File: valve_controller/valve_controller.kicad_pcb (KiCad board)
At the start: 2 copper layers, 9 parts, among them U1 LAN8720A, U2 ADS1115IDGS, U3 MCP4728, U5 LM2596S-5, U6 LDO-LM7805MPX/NOPB, U7 ESP32-S3, U8 TVS-SMDB03CE3

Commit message: First layout  of pcb
Ready for review
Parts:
- added C1: 100nF, Capacitor_SMD:C_0805_2012Metric_Pad1.18x1.45mm_HandSolder, F.Cu at (106.3, 51.9)
- added C2: 100nF, Capacitor_SMD:C_0805_2012Metric_Pad1.18x1.45mm_HandSolder, F.Cu at (106.3, 54.9)
- added J10: 643260100604, 643260100604:643260100604, F.Cu at (182.2, 140.5)
- added J11: 643260100604, 643260100604:643260100604, F.Cu at (182.2, 120.8)
- added J4: 643260100604, 643260100604:643260100604, F.Cu at (117.1, 140.5)
- added J5: 643260100604, 643260100604:643260100604, F.Cu at (117.1, 120.8)
- added J6: 643260100604, 643260100604:643260100604, F.Cu at (138.8, 140.5)
- added J7: 643260100604, 643260100604:643260100604, F.Cu at (138.8, 120.8)
- added J8: 643260100604, 643260100604:643260100604, F.Cu at (160.5, 140.5)
- added J9: 643260100604, 643260100604:643260100604, F.Cu at (160.5, 120.8)
- added R10: 1k, Resistor_SMD:R_0201_0603Metric, F.Cu at (109.9, 51.3)
- added R11: 1k, Resistor_SMD:R_0201_0603Metric, F.Cu at (109.9, 53.0)
- added SW1: TS09-63-25-WT-160-SMT-TR, Button_Switch_SMD:SW_DIP_SPSTx01_Slide_6.7x4.1mm_W8.61mm_P2.54mm_LowProfile, F.Cu at (110.2, 41.6)
- added SW2: TS09-63-25-WT-160-SMT-TR, Button_Switch_SMD:SW_DIP_SPSTx01_Slide_6.7x4.1mm_W8.61mm_P2.54mm_LowProfile, F.Cu at (110.2, 47.5)
- moved D1 24.7 mm to (181.0, 89.5)
- moved D2 24.7 mm to (181.0, 95.0)
- moved U1 24.7 mm to (154.5, 90.5)
- moved U2 24.7 mm to (148.8, 76.5)
- moved U3 24.7 mm to (153.4, 83.0)
- moved U5 24.7 mm to (138.4, 73.7)
- moved U6 24.7 mm to (168.8, 74.6)
- moved U7 24.7 mm to (161.5, 83.8)
- moved U8 24.7 mm to (157.0, 70.6)
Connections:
- U1 pad 5: unconnected-(U1-XTAL1/CLKIN-Pad5) -> /25MHZ
- U2 pad 10: /SCL_ADC1 -> /SCL
- U2 pad 2: /ALERT/RDY_ADC1 -> unconnected-(U2-ALERT/RDY-Pad2)
- U2 pad 9: /SDA_ADC1 -> /SDA
- U3 pad 2: /SCL_DAC1 -> /SCL
- U3 pad 3: /SDA_DAC1 -> /SDA
- U3 pad 5: /RDY_DAC1 -> unconnected-(U3-RDY/~{BSY}-Pad5)
- U7 pad 2: Net-(U7-VDD3P3-Pad2) -> +3V3
- U7 pad 20: unconnected-(U7-VDD3P3_RTC-Pad20) -> +3V3
- U7 pad 3: Net-(U7-VDD3P3-Pad2) -> +3V3
- U7 pad 38: unconnected-(U7-GPIO33-Pad38) -> /SCL
- U7 pad 39: unconnected-(U7-GPIO34-Pad39) -> /SDA
- U7 pad 4: unconnected-(U7-CHIP_PU-Pad4) -> /CHIP_PU
- U7 pad 55: Net-(U7-VDDA-Pad55) -> +3V3
- U7 pad 56: Net-(U7-VDDA-Pad55) -> +3V3

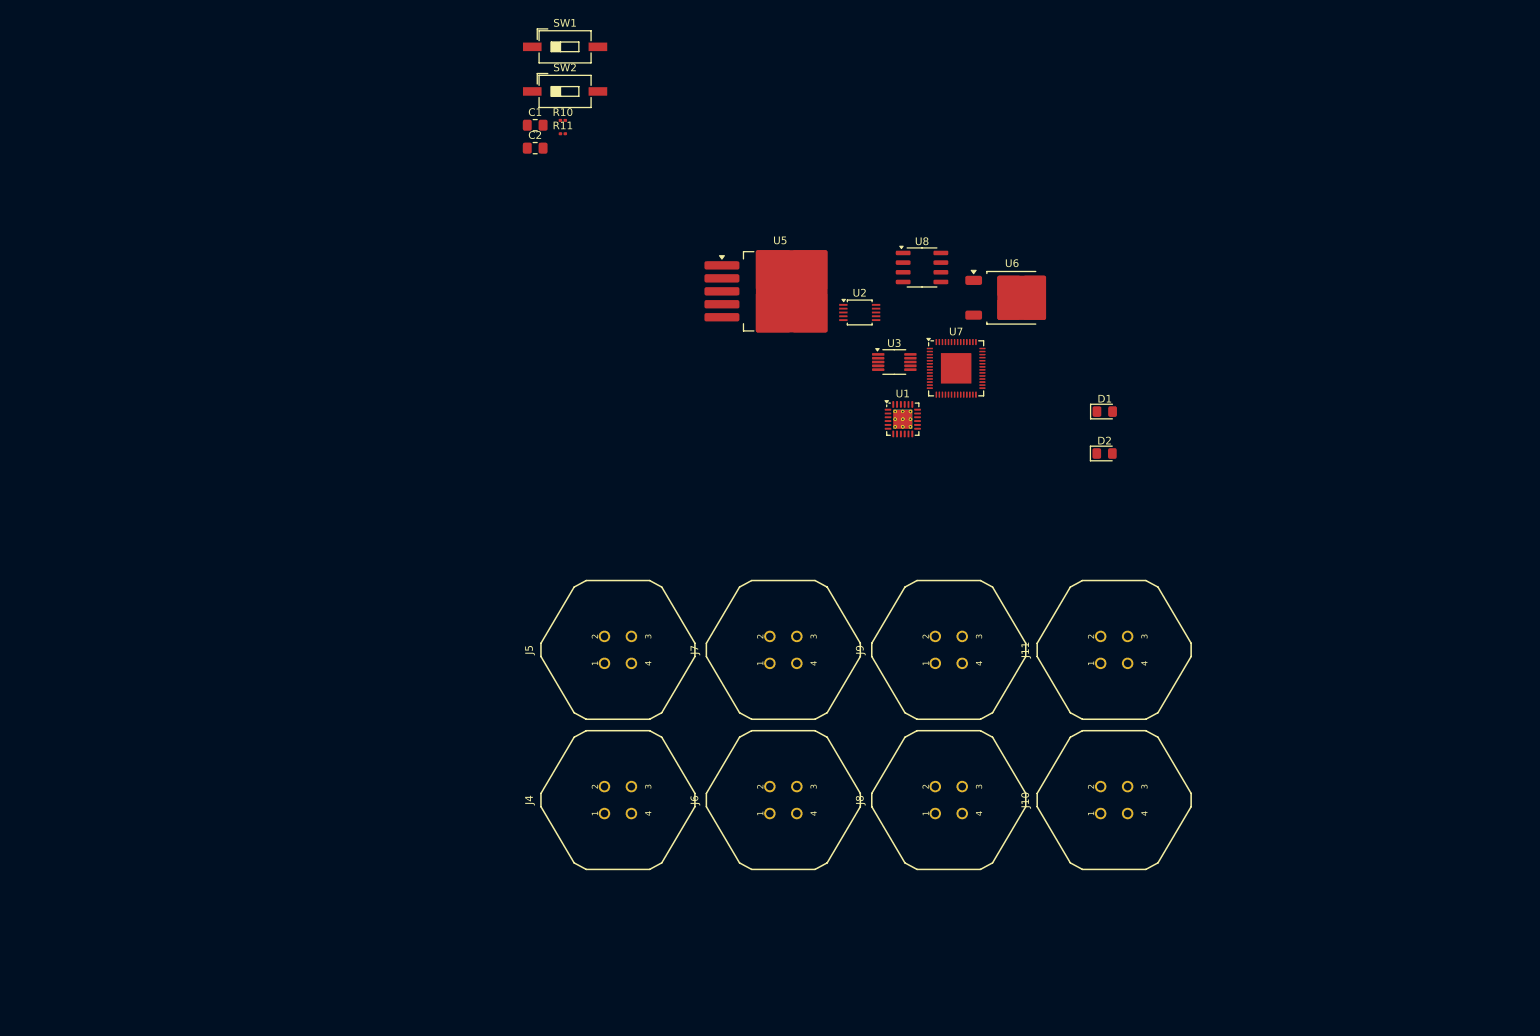
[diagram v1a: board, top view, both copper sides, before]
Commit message: Updated + ports
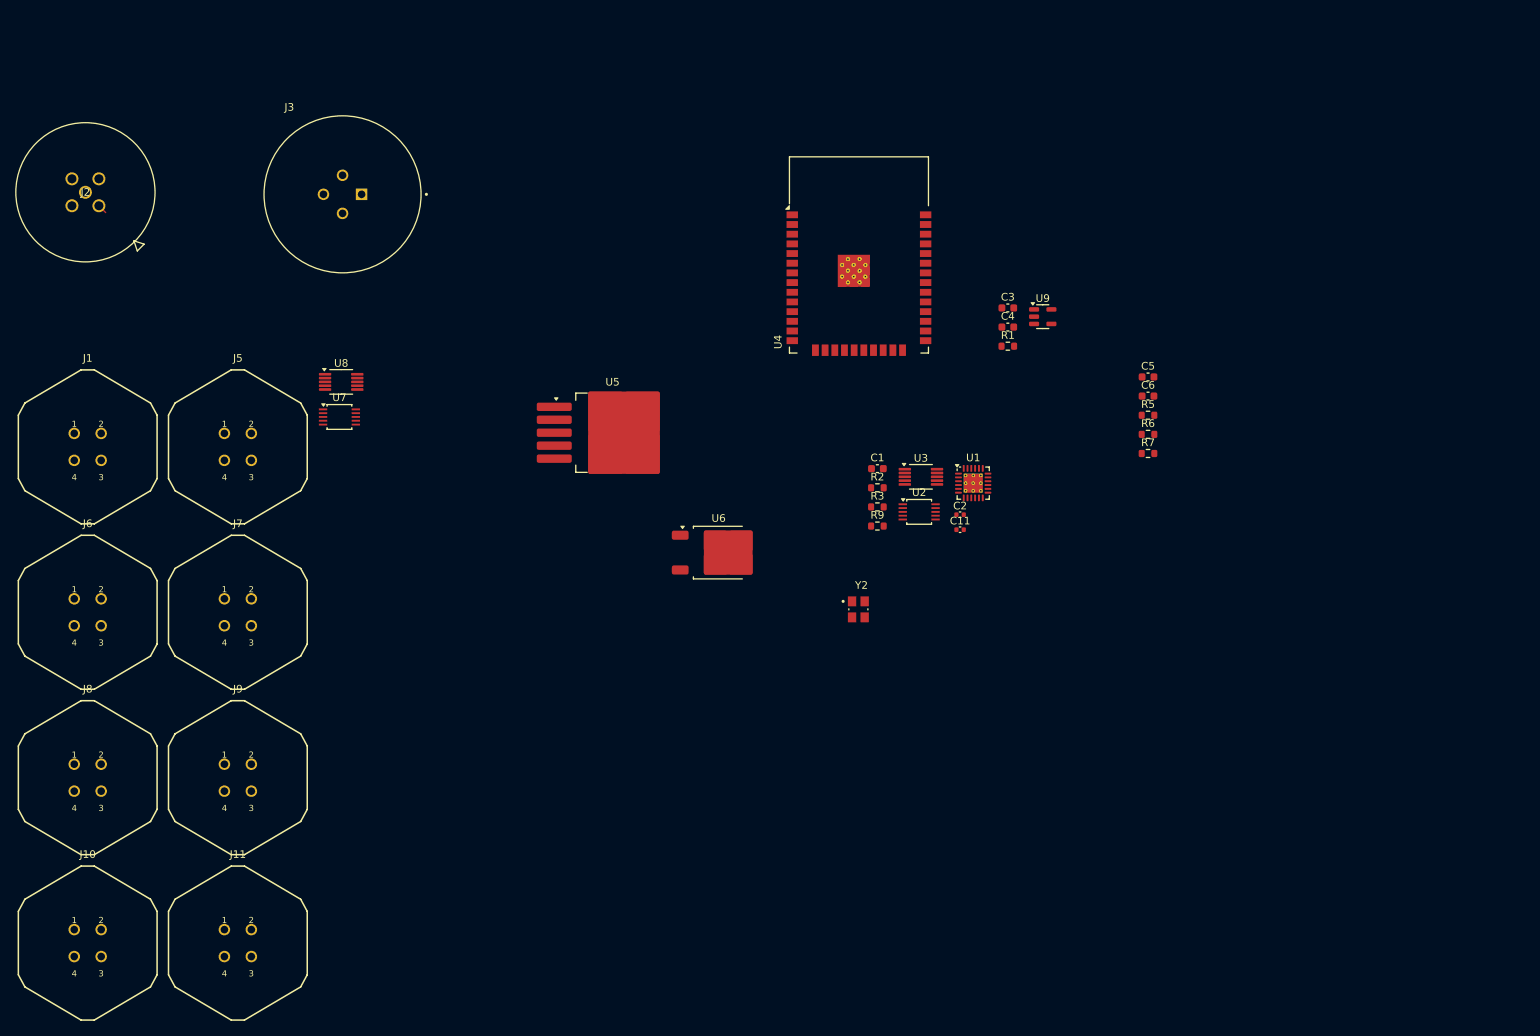
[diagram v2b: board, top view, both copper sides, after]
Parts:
- removed D1, D2: LED, LED_SMD:LED_0805_2012Metric_Pad1.15x1.40mm_HandSolder
- removed J4: 643260100604, 643260100604:643260100604
- removed R10, R11: 1k, Resistor_SMD:R_0201_0603Metric
- removed SW1, SW2: TS09-63-25-WT-160-SMT-TR, Button_Switch_SMD:SW_DIP_SPSTx01_Slide_6.7x4.1mm_W8.61mm_P2.54mm_LowProfile
- added C11: 0.1uF, Capacitor_SMD:C_0402_1005Metric, F.Cu at (162.0, 105.0)
- added C3: 22uF, Capacitor_SMD:C_0603_1608Metric, F.Cu at (168.3, 75.9)
- added C4: 22uF, Capacitor_SMD:C_0603_1608Metric, F.Cu at (168.3, 78.4)
- added C5: 1uF, Capacitor_SMD:C_0603_1608Metric, F.Cu at (186.7, 85.0)
- added C6: 470pF, Capacitor_SMD:C_0603_1608Metric, F.Cu at (186.7, 87.5)
- added J1: 643260100604, 643260100604:643260100604, F.Cu at (47.6, 94.1)
- added J2: T4143512051-000, T4143512051_000:CONN5_T4143512051, F.Cu at (45.5, 59.0)
- added J3: M12A-04PMMP-SF8001, M12A-04PMMP-SF8001:AMPHENOL_M12A-04PMMP-SF8001, F.Cu at (81.0, 61.0)
- added R1: 100k, Resistor_SMD:R_0603_1608Metric, F.Cu at (168.3, 80.9)
- added R2: 100k, Resistor_SMD:R_0603_1608Metric, F.Cu at (151.2, 99.5)
- added R3: 100k, Resistor_SMD:R_0603_1608Metric, F.Cu at (151.2, 102.0)
- added R5: 12.1k, Resistor_SMD:R_0603_1608Metric, F.Cu at (186.7, 90.0)
- added R6: 10k, Resistor_SMD:R_0603_1608Metric, F.Cu at (186.7, 92.5)
- added R7: 10k, Resistor_SMD:R_0603_1608Metric, F.Cu at (186.7, 95.0)
- added R9: 100k, Resistor_SMD:R_0603_1608Metric, F.Cu at (151.2, 104.5)
- added U4: ESP32-WROOM-32, RF_Module:ESP32-WROOM-32, F.Cu at (148.8, 71.9)
- added U9: AP2112K-3.3, Package_TO_SOT_SMD:SOT-23-5, F.Cu at (172.9, 77.0)
- added Y2: ASE-25.000MHZ-LC-T, ASE-25.000MHZ-LC-T:XTAL_ASE-25.000MHZ-LC-T, F.Cu at (148.7, 115.5)
- C1: value 100nF -> 22uF; footprint Capacitor_SMD:C_0805_2012Metric_Pad1.18x1.45mm_HandSolder -> Capacitor_SMD:C_0603_1608Metric
- C2: value 100nF -> 0.1uF; footprint Capacitor_SMD:C_0805_2012Metric_Pad1.18x1.45mm_HandSolder -> Capacitor_SMD:C_0402_1005Metric
- U7: value ESP32-S3 -> ADS1115IDGS; footprint Package_DFN_QFN:QFN-56-1EP_7x7mm_P0.4mm_EP4x4mm -> Package_SO:TSSOP-10_3x3mm_P0.5mm
- U8: value TVS-SMDB03CE3 -> MCP4728; footprint Package_SO:SOIC-8_3.9x4.9mm_P1.27mm -> Package_SO:MSOP-10_3x3mm_P0.5mm
- moved J10 136.0 mm to (47.6, 159.2), turned to 0 degrees
- moved J11 121.2 mm to (67.3, 159.2), turned to 0 degrees
- moved J8 113.0 mm to (47.6, 137.5), turned to 0 degrees
- moved J9 94.8 mm to (67.3, 137.5), turned to 0 degrees
- moved J6 94.5 mm to (47.6, 115.8), turned to 0 degrees
- moved U7 81.2 mm to (80.6, 90.2)
- moved U8 77.7 mm to (80.8, 85.6)
- moved C2 73.6 mm to (162.0, 103.0)
- moved J7 71.7 mm to (67.3, 115.8), turned to 0 degrees
- moved C1 63.6 mm to (151.2, 97.0)
- moved J5 56.5 mm to (67.3, 94.1), turned to 0 degrees
- moved U6 51.0 mm to (130.3, 108.0)
- moved U5 28.8 mm to (116.4, 92.3)
- moved U2 27.3 mm to (156.7, 102.7)
- moved U3 15.5 mm to (156.9, 98.1)
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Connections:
- C1 pad 1: GND -> +3V3
- C1 pad 2: /BOOT -> GND
- C2 pad 1: GND -> +3V3
- C2 pad 2: /CHIP_PU -> GND
- J10 pad 1: unconnected-(J10-Pad1) -> /AIN2_ADC1
- J10 pad 4: unconnected-(J10-Pad4) -> /ANOUT2_DAC1
- J11 pad 1: unconnected-(J11-Pad1) -> /AIN3_ADC1
- J11 pad 4: unconnected-(J11-Pad4) -> /ANOUT3_DAC1
- J5 pad 1: unconnected-(J5-Pad1) -> /AIN0_ADC0
- J5 pad 4: unconnected-(J5-Pad4) -> /ANOUT0_DAC0
- J6 pad 1: unconnected-(J6-Pad1) -> /AIN2_ADC0
- J6 pad 4: unconnected-(J6-Pad4) -> /ANOUT2_DAC0
- J7 pad 1: unconnected-(J7-Pad1) -> /AIN3_ADC0
- J7 pad 4: unconnected-(J7-Pad4) -> /ANOUT3_DAC0
- J8 pad 1: unconnected-(J8-Pad1) -> /AIN0_ADC1
- J8 pad 4: unconnected-(J8-Pad4) -> /ANOUT0_DAC1
- J9 pad 1: unconnected-(J9-Pad1) -> /AIN1_ADC1
- J9 pad 4: unconnected-(J9-Pad4) -> /ANOUT1_DAC1
- U2 pad 4: /AIN0_ADC1 -> /AIN0_ADC0
- U2 pad 5: /AIN1_ADC1 -> /AIN1_ADC0
- U2 pad 6: /AIN2_ADC1 -> /AIN2_ADC0
- U2 pad 7: /AIN3_ADC1 -> /AIN3_ADC0
- U3 pad 6: /ANOUT0_DAC1 -> /ANOUT0_DAC0
- U3 pad 7: /ANOUT1_DAC1 -> /ANOUT1_DAC0
- U3 pad 8: /ANOUT2_DAC1 -> /ANOUT2_DAC0
- U3 pad 9: /ANOUT3_DAC1 -> /ANOUT3_DAC0
- U7 pad 1: unconnected-(U7-LNA_IN-Pad1) -> GND
- U7 pad 10: unconnected-(U7-GPIO5-Pad10) -> /SCL
- U7 pad 2: +3V3 -> unconnected-(U7-ALERT/RDY-Pad2)
- U7 pad 3: +3V3 -> GND
- U7 pad 4: /CHIP_PU -> /AIN0_ADC1
- U7 pad 5: /REF_CLK -> /AIN1_ADC1
- U7 pad 6: unconnected-(U7-GPIO1-Pad6) -> /AIN2_ADC1
- U7 pad 7: unconnected-(U7-GPIO2-Pad7) -> /AIN3_ADC1
- U7 pad 8: unconnected-(U7-GPIO3-Pad8) -> +3V3
- U7 pad 9: unconnected-(U7-GPIO4-Pad9) -> /SDA
- U8 pad 1: +5V -> +3V3
- U8 pad 2: /USB_N -> /SCL
- U8 pad 3: /USB_P -> /SDA
- U8 pad 4: unconnected-(U8-Pad4) -> GND
- U8 pad 5: GND -> unconnected-(U8-RDY/~{BSY}-Pad5)
- U8 pad 6: GND -> /ANOUT0_DAC1
- U8 pad 7: GND -> /ANOUT1_DAC1
- U8 pad 8: GND -> /ANOUT2_DAC1

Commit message: Started pcb layout
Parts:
- removed U6: LDO-LM7805MPX/NOPB, Package_TO_SOT_SMD:TO-252-2
- added D1: WS2812B, LED_SMD:LED_WS2812B_PLCC4_5.0x5.0mm_P3.2mm, F.Cu at (156.7, 105.3)
- moved J2 137.0 mm to (182.5, 62.0)
- moved J11 126.8 mm to (139.8, 55.2), turned to 90 degrees
- moved J3 120.3 mm to (185.0, 121.5), turned to 180 degrees
- moved J10 98.7 mm to (139.2, 122.8), turned to 90 degrees
- moved J9 95.6 mm to (115.8, 55.2), turned to 90 degrees
- moved U7 75.9 mm to (153.4, 68.9), turned to 180 degrees
- moved J8 69.3 mm to (115.2, 122.8), turned to 90 degrees
- moved U8 67.0 mm to (146.6, 72.5), turned to 180 degrees
- moved J7 65.2 mm to (91.3, 55.2), turned to 90 degrees
- moved U5 61.0 mm to (176.6, 102.2), turned to 180 degrees
- moved J6 43.5 mm to (90.5, 122.8), turned to 90 degrees
- moved Y2 41.6 mm to (169.9, 79.8)
- moved J5 38.9 mm to (66.3, 55.2), turned to 90 degrees
- moved U2 35.3 mm to (146.6, 68.8)
- moved J1 33.8 mm to (65.5, 122.8), turned to 90 degrees
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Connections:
- J2 pad 2: /RX_N -> /RX_P
- U4 pad 13: /RXER -> /TXD0
- U4 pad 14: /MDIO -> /TXEN
- U4 pad 16: /CRS_DV -> /TXD1
- U4 pad 23: /RXD1 -> /MDIO
- U4 pad 24: unconnected-(U4-IO2-Pad24) -> /CRS_DV
- U4 pad 26: unconnected-(U4-IO4-Pad26) -> /RXER
- U4 pad 27: /RXD0 -> unconnected-(U4-IO16-Pad27)
- U4 pad 28: /TXEN -> unconnected-(U4-IO17-Pad28)
- U4 pad 29: /MDC -> unconnected-(U4-IO5-Pad29)
- U4 pad 30: /TXD1 -> unconnected-(U4-IO18-Pad30)
- U4 pad 31: /TXD0 -> unconnected-(U4-IO19-Pad31)
- U4 pad 34: /ESP_RX -> unconnected-(U4-RXD0/IO3-Pad34)
- U4 pad 35: /ESP_TX -> unconnected-(U4-TXD0/IO1-Pad35)
- U4 pad 36: unconnected-(U4-IO22-Pad36) -> /SCL
- U4 pad 37: unconnected-(U4-IO23-Pad37) -> /SDA
- U4 pad 6: /SDA -> unconnected-(U4-IO34-Pad6)
- U4 pad 9: /SCL -> unconnected-(U4-IO33-Pad9)
- U5 pad 4: +5V -> unconnected-(U5-FB-Pad4)
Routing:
- net +5V: track 0.00 -> 22.0 mm
- net +3V3: track 0.00 -> 21.9 mm
- net GND: track 0.00 -> 16.3 mm, vias 0 -> 5
- net /25MHZ: track 0.00 -> 6.32 mm
- net /ESP_EN: track 0.00 -> 3.99 mm
- net /SDA: track 0.00 -> 3.82 mm
- net Net-(U1-LED2/~{INTSEL}): track 0.00 -> 3.41 mm
- net Net-(U1-VDDCR): track 0.00 -> 3.30 mm
- net Net-(U1-RBIAS): track 0.00 -> 2.55 mm
- net Net-(U9-EN): track 0.00 -> 1.91 mm
- net /SCL: track 0.00 -> 1.80 mm
- net Net-(U1-~{RST}): track 0.00 -> 1.72 mm
- net unconnected-(U4-IO34-Pad6): track 0.00 -> 0.53 mm
- net /TXD0: track 0.00 -> 0.53 mm
